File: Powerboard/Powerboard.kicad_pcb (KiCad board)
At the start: 2 copper layers, 44 parts, among them IC1 TEENSY_4.1, J1 Screw_Terminal_01x02, J3 Screw_Terminal_01x12, J4 Screw_Terminal_01x06, J5 Screw_Terminal_01x06, J6 Screw_Terminal_01x06, J7 Screw_Terminal_01x12, U1 MP2338GTL-Z, U3 MP2338GTL-Z, U5 SN74HCT245N, U6 SN74HCT245N, U7 SN74LVC245AN, U8 SN74LVC245AN

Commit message: Updated
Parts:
- removed C13: 100nF, Capacitor_SMD:C_0603_1608Metric
- removed C17, C19: 0.1uF, Capacitor_SMD:C_0603_1608Metric
- removed C18: 22nF, Capacitor_SMD:C_0603_1608Metric
- removed C20: 22uF, Capacitor_SMD:C_1206_3216Metric
- removed C21: 22uF, Capacitor_SMD:C_0603_1608Metric
- removed C22: 300pF, Capacitor_SMD:C_0603_1608Metric
- removed J7: Screw_Terminal_01x12, TerminalBlock_Phoenix:TerminalBlock_Phoenix_MKDS-1,5-12-5.08_1x12_P5.08mm_Horizontal
- removed L3: 6.8uH, Inductor_SMD:L_Bourns_SRP7028A_7.3x6.6mm
- removed R13: 191k, Resistor_SMD:R_0603_1608Metric
- removed R14: 49.9k, Resistor_SMD:R_0603_1608Metric
- removed R15, R16, R17: 10k, Resistor_SMD:R_0603_1608Metric
- removed R18: 90.9k, Resistor_SMD:R_0603_1608Metric
- removed R5: 9.09k, Resistor_SMD:R_0603_1608Metric
- removed R6: 51k, Resistor_SMD:R_0603_1608Metric
- removed U5, U6: SN74HCT245N, SN74HCT245N:N20
- removed U7, U8: SN74LVC245AN, SN74LVC245AN:N20
- added C10: 22uF, Capacitor_SMD:C_1206_3216Metric, F.Cu at (72.2, 87.5)
- added C9: 22uF, Capacitor_SMD:C_1206_3216Metric, F.Cu at (75.5, 87.5)
- added IC2: AP63301WU-7, AP63301WU:SOT95P280X100-6N, F.Cu at (61.5, 120.0)
- added IC3: AP63301WU-7, AP63301WU:SOT95P280X100-6N, F.Cu at (63.0, 90.0)
- added J2: Screw_Terminal_01x02, TerminalBlock_Altech:Altech_AK100_1x02_P5.00mm, F.Cu at (63.0, 140.0)
- added L2: 4.7uH, Inductor_SMD:L_Bourns_SRP7028A_7.3x6.6mm, F.Cu at (66.0, 82.0)
- added U2: SN74HCT245N, SN74HCT245N:N20, F.Cu at (169.8, 122.4)
- added U4: SN74LVC245AN, SN74LVC245AN:N20, F.Cu at (146.7, 122.4)
- C1: footprint Capacitor_SMD:C_1206_3216Metric -> Capacitor_SMD:C_1210_3225Metric
- C11: value 22uF -> 100nF; footprint Capacitor_SMD:C_1206_3216Metric -> Capacitor_SMD:C_0603_1608Metric
- C2: value 10uF -> 0.1uF; footprint Capacitor_SMD:C_1206_3216Metric -> Capacitor_SMD:C_0603_1608Metric
- C3: value 0.1uF -> 47pf
- C4: value 22nF -> 22uF; footprint Capacitor_SMD:C_0603_1608Metric -> Capacitor_SMD:C_1206_3216Metric
- C5: value 0.1uF -> 22uF; footprint Capacitor_SMD:C_0603_1608Metric -> Capacitor_SMD:C_1206_3216Metric
- C6: value 22uF -> 10uF; footprint Capacitor_SMD:C_1206_3216Metric -> Capacitor_SMD:C_1210_3225Metric
- C7: value 22uF -> 0.1uF; footprint Capacitor_SMD:C_1206_3216Metric -> Capacitor_SMD:C_0603_1608Metric
- C8: value 470pF -> 56pf; footprint Capacitor_SMD:C_0603_1608Metric -> Capacitor_SMD:C_0201_0603Metric
- J1: value Screw_Terminal_01x02 -> Screw_Terminal_01x06; footprint TerminalBlock_Altech:Altech_AK100_1x02_P5.00mm -> TerminalBlock_Phoenix:TerminalBlock_Phoenix_MPT-0,5-6-2.54_1x06_P2.54mm_Horizontal
- J3: value Screw_Terminal_01x12 -> 1993776; footprint TerminalBlock_Phoenix:TerminalBlock_Phoenix_MKDS-1,5-12-5.08_1x12_P5.08mm_Horizontal -> 1993776:PHOENIX_1993776
- J4, J5: value Screw_Terminal_01x06 -> Screw_Terminal_01x12; footprint TerminalBlock_Phoenix:TerminalBlock_Phoenix_MKDS-1,5-6_1x06_P5.00mm_Horizontal -> TerminalBlock_Phoenix:TerminalBlock_Phoenix_MPT-0,5-12-2.54_1x12_P2.54mm_Horizontal
- J6: value Screw_Terminal_01x06 -> 1993776; footprint TerminalBlock_Phoenix:TerminalBlock_Phoenix_MKDS-1,5-6_1x06_P5.00mm_Horizontal -> 1993776:PHOENIX_1993776
- R1: value 191k -> 30.1k
- R2: value 49.9k -> 158k
- R3: value 100k -> 30.1k
- R4: value 10k -> 93.1k
- U1: value MP2338GTL-Z -> SN74HCT245N; footprint MP2338GTL:SOT583_MP2338_MNP -> SN74HCT245N:N20
- U3: value MP2338GTL-Z -> SN74LVC245AN; footprint MP2338GTL:SOT583_MP2338_MNP -> SN74LVC245AN:N20
- moved C7 127.9 mm to (59.0, 84.5), turned to 90 degrees
- moved C2 123.0 mm to (56.5, 116.0), turned to 90 degrees
- moved R3 119.4 mm to (58.5, 91.5)
- moved R4 119.4 mm to (58.5, 94.0), turned to 180 degrees
- moved C6 117.5 mm to (65.5, 95.5)
- moved R2 116.8 mm to (58.0, 123.5), turned to 180 degrees
- moved C1 115.7 mm to (64.0, 125.5)
- moved C8 115.5 mm to (58.5, 96.7), turned to 180 degrees
- moved C3 113.0 mm to (58.0, 126.5), turned to 180 degrees
- moved R1 112.8 mm to (57.9, 121.3)
- moved L1 109.0 mm to (64.5, 112.5)
- moved C5 100.3 mm to (70.5, 115.5), turned to -90 degrees
- moved C4 96.7 mm to (74.0, 115.5), turned to -90 degrees
- moved J6 78.2 mm to (175.3, 85.9)
- moved C11 73.1 mm to (173.3, 98.0)
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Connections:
- C11 pad 1: /Step_down_3v3/Vin -> /Vout_5v
- C2 pad 1: /Step_down_3v3/Vin -> Net-(IC2-BST)
- C2 pad 2: GND -> Net-(IC2-SW)
- C3 pad 1: /Step_down_3v3/Vin -> Net-(IC2-FB)
- C3 pad 2: GND -> /Vout_5v
- C4 pad 1: Net-(U1-SS) -> /Vout_5v
- C5 pad 1: Net-(U1-SW) -> /Vout_5v
- C5 pad 2: Net-(U1-BST) -> GND
- C6 pad 1: /Vout_3v3 -> /Step_down_3v3/Vin
- C7 pad 1: /Vout_3v3 -> Net-(IC3-BST)
- C7 pad 2: GND -> Net-(IC3-SW)
- C8 pad 1: Net-(C8-Pad1) -> Net-(IC3-FB)
- J1 pad 1: /Step_down_3v3/Vin -> /SW1
- J1 pad 2: GND -> /SW2
- J4 pad 1: /Vout_3v3 -> /Motor Driver1/PUL1_5V
- J4 pad 2: /Vout_3v3 -> /Motor Driver1/DIR1_5v
- J4 pad 3: /Vout_3v3 -> /Motor Driver1/PUL2_5v
- J4 pad 4: /Vout_3v3 -> /Motor Driver1/DIR2_5v
- J4 pad 5: /Vout_3v3 -> /Motor Driver1/PUL3_5v
- J4 pad 6: /Vout_3v3 -> /Motor Driver1/DIR3_5v
- J5 pad 1: /SW1 -> /Encoder data1/EA1_5v
- J5 pad 2: /SW2 -> /Encoder data1/EB1_5v
- J5 pad 3: /SW3 -> /Encoder data1/EA2_5v
- J5 pad 4: /SW4 -> /Encoder data1/EB2_5v
- J5 pad 5: /SW5 -> /Encoder data1/EA3_5v
- J5 pad 6: /SW6 -> /Encoder data1/EB3_5v
- L1 pad 1: Net-(U1-SW) -> Net-(IC2-SW)
- L1 pad 2: /Vout_3v3 -> /Vout_5v
- R1 pad 1: /Step_down_3v3/Vin -> GND
- R1 pad 2: Net-(U1-EN) -> Net-(IC2-FB)
- R2 pad 1: Net-(U1-EN) -> Net-(IC2-FB)
- R2 pad 2: GND -> /Vout_5v
- R3 pad 1: Net-(U1-PG) -> GND
- R3 pad 2: /Vout_3v3 -> Net-(IC3-FB)
- R4 pad 1: Net-(C8-Pad1) -> Net-(IC3-FB)
- R4 pad 2: Net-(U1-FB) -> /Vout_3v3
- U1 pad 1: Net-(U1-PG) -> /Vout_5v
- U1 pad 2: /Step_down_3v3/Vin -> /PUL_1_3v3
- U1 pad 3: Net-(U1-SW) -> /DIR_1_3v3
- U1 pad 4: GND -> /PUL_2_3v3
- U1 pad 5: Net-(U1-BST) -> /DIR_2_3v3
- U1 pad 6: Net-(U1-EN) -> /PUL_3_3v3
- U1 pad 7: Net-(U1-SS) -> /DIR_3_3v3
- U1 pad 8: Net-(U1-FB) -> /PUL_4_3v3
- U3 pad 1: Net-(U3-PG) -> GND
- U3 pad 2: /Step_down_3v3/Vin -> /EA1_3v3
- U3 pad 3: Net-(U3-SW) -> /EB1_3v3
- U3 pad 4: GND -> /EA2_3v3
- U3 pad 5: Net-(U3-BST) -> /EB2_3v3
- U3 pad 6: Net-(U3-EN) -> /EA3_3v3
- U3 pad 7: Net-(U3-SS) -> /EB3_3v3
- U3 pad 8: Net-(U3-FB) -> /EA4_3v3
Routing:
- net /Step_down_3v3/Vin: track 0.00 -> 57.5 mm, vias 0 -> 1
- net /Vout_3v3: track 0.00 -> 29.2 mm, vias 0 -> 2
- net /Vout_5v: track 0.00 -> 28.4 mm, vias 0 -> 2
- net GND: vias 0 -> 21
- added copper zone on F.Cu, net (none)
- added copper zone on F.Cu, net /Step_down_3v3/Vin
- added copper zone on F.Cu, net /Vout_3v3
- added copper zone on F.Cu, net /Vout_5v
- added copper zone on B.Cu, net GND
- added copper zone on F.Cu, net Net-(IC2-BST)
- added copper zone on F.Cu, net Net-(IC2-FB)
- added copper zone on F.Cu, net Net-(IC2-SW)
- added copper zone on F.Cu, net Net-(IC3-BST)
- added copper zone on F.Cu, net Net-(IC3-FB)
- added copper zone on F.Cu, net Net-(IC3-SW)

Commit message: update
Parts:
- added H1: MountingHole, MountingHole:MountingHole_3.2mm_M3_Pad_Via, F.Cu at (51.5, 142.0)
- added H2: MountingHole, MountingHole:MountingHole_3.2mm_M3_Pad_Via, F.Cu at (140.2, 60.2)
- added H3: MountingHole, MountingHole:MountingHole_3.2mm_M3_Pad_Via, F.Cu at (214.5, 142.0)
- added H4: MountingHole, MountingHole:MountingHole_3.2mm_M3_Pad_Via, F.Cu at (214.2, 59.2)
- U1, U2: value SN74HCT245N -> SN74HCT245NSR; footprint SN74HCT245N:N20 -> SN74HCT245NSR:NS20
- U3, U4: value SN74LVC245AN -> SN74LVC245ADW; footprint SN74LVC245AN:N20 -> SN74LVC245ADW:DW20
- moved J1 81.9 mm to (192.4, 140.0)
- moved J5 78.1 mm to (81.4, 140.5)
- moved J4 69.7 mm to (124.8, 140.0)
- moved J6 58.5 mm to (177.1, 144.3)
- moved J3 58.0 mm to (163.1, 143.8)
- moved U3 47.1 mm to (89.0, 123.0), turned to -90 degrees
- moved U4 41.2 mm to (105.5, 123.0), turned to -90 degrees
- moved IC1 26.8 mm to (150.9, 85.1)
- moved U1 26.1 mm to (133.2, 120.6), turned to -90 degrees
- moved U2 20.4 mm to (149.5, 121.0), turned to -90 degrees
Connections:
- U1 pad 11: /Motor Driver1/DIR4_5v -> /Motor Driver1/PUL1_5V
- U1 pad 12: /Motor Driver1/PUL4_5v -> /Motor Driver1/DIR1_5v
- U1 pad 13: /Motor Driver1/DIR3_5v -> /Motor Driver1/PUL2_5v
- U1 pad 14: /Motor Driver1/PUL3_5v -> /Motor Driver1/DIR2_5v
- U1 pad 15: /Motor Driver1/DIR2_5v -> /Motor Driver1/PUL3_5v
- U1 pad 16: /Motor Driver1/PUL2_5v -> /Motor Driver1/DIR3_5v
- U1 pad 17: /Motor Driver1/DIR1_5v -> /Motor Driver1/PUL4_5v
- U1 pad 18: /Motor Driver1/PUL1_5V -> /Motor Driver1/DIR4_5v
- U1 pad 2: /PUL_1_3v3 -> /DIR_4_3v3
- U1 pad 3: /DIR_1_3v3 -> /PUL_4_3v3
- U1 pad 4: /PUL_2_3v3 -> /DIR_3_3v3
- U1 pad 5: /DIR_2_3v3 -> /PUL_3_3v3
- U1 pad 6: /PUL_3_3v3 -> /DIR_2_3v3
- U1 pad 7: /DIR_3_3v3 -> /PUL_2_3v3
- U1 pad 8: /PUL_4_3v3 -> /DIR_1_3v3
- U1 pad 9: /DIR_4_3v3 -> /PUL_1_3v3
- U2 pad 15: /Motor Driver1/DIR6_5v -> /Motor Driver1/PUL5_5v
- U2 pad 16: /Motor Driver1/PUL6_5v -> /Motor Driver1/DIR5_5v
- U2 pad 17: /Motor Driver1/DIR5_5v -> /Motor Driver1/PUL6_5v
- U2 pad 18: /Motor Driver1/PUL5_5v -> /Motor Driver1/DIR6_5v
- U2 pad 2: /PUL_5_3v3 -> /DIR_6_3v3
- U2 pad 3: /DIR_5_3v3 -> /PUL_6_3v3
- U2 pad 4: /PUL_6_3v3 -> /DIR_5_3v3
- U2 pad 5: /DIR_6_3v3 -> /PUL_5_3v3
- U3 pad 11: /Encoder data1/EB4_5v -> /Encoder data1/EA1_5v
- U3 pad 12: /Encoder data1/EA4_5v -> /Encoder data1/EB1_5v
- U3 pad 13: /Encoder data1/EB3_5v -> /Encoder data1/EA2_5v
- U3 pad 14: /Encoder data1/EA3_5v -> /Encoder data1/EB2_5v
- U3 pad 15: /Encoder data1/EB2_5v -> /Encoder data1/EA3_5v
- U3 pad 16: /Encoder data1/EA2_5v -> /Encoder data1/EB3_5v
- U3 pad 17: /Encoder data1/EB1_5v -> /Encoder data1/EA4_5v
- U3 pad 18: /Encoder data1/EA1_5v -> /Encoder data1/EB4_5v
- U3 pad 2: /EA1_3v3 -> /EB4_3v3
- U3 pad 3: /EB1_3v3 -> /EA4_3v3
- U3 pad 4: /EA2_3v3 -> /EB3_3v3
- U3 pad 5: /EB2_3v3 -> /EA3_3v3
- U3 pad 6: /EA3_3v3 -> /EB2_3v3
- U3 pad 7: /EB3_3v3 -> /EA2_3v3
- U3 pad 8: /EA4_3v3 -> /EB1_3v3
- U3 pad 9: /EB4_3v3 -> /EA1_3v3
- U4 pad 15: /Encoder data1/EB6_5v -> /Encoder data1/EA5_5v
- U4 pad 16: /Encoder data1/EA6_5v -> /Encoder data1/EB5_5v
- U4 pad 17: /Encoder data1/EB5_5v -> /Encoder data1/EA6_5v
- U4 pad 18: /Encoder data1/EA5_5v -> /Encoder data1/EB6_5v
- U4 pad 2: /EA5_3v3 -> /EB6_3v3
- U4 pad 3: /EB5_3v3 -> /EA6_3v3
- U4 pad 4: /EA6_3v3 -> /EB5_3v3
- U4 pad 5: /EB6_3v3 -> /EA5_3v3
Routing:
- net /Step_down_3v3/Vin: track 57.5 -> 55.0 mm
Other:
- board outline added: 170 x 90 mm

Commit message: Pre-DRC Done
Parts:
- H1, H2, H3, H4: footprint MountingHole:MountingHole_3.2mm_M3_Pad_Via -> MountingHole:MountingHole_3.2mm_M3_Pad
- moved C11 56.0 mm to (128.1, 131.0), turned to 180 degrees
- moved C12 41.9 mm to (145.1, 131.5), turned to 180 degrees
- moved IC1 14.8 mm to (143.9, 98.1)
- moved U1 10.9 mm to (122.7, 123.6)
- moved U2 10.2 mm to (139.6, 123.5)
- moved J4 8.26 mm to (116.6, 140.5)
- moved J6 7.05 mm to (170.1, 143.8)
- moved J3 7.00 mm to (156.1, 143.8)
- moved J2 0.50 mm to (63.0, 139.5)
- moved U4 0.50 mm to (106.0, 123.0)
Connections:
- IC1 pad 16: /EB4_3v3 -> /EA1_3v3
- IC1 pad 17: /EA4_3v3 -> /EB1_3v3
- IC1 pad 18: /EB3_3v3 -> /EA2_3v3
- IC1 pad 19: /EA3_3v3 -> /EB2_3v3
- IC1 pad 20: /EB2_3v3 -> /EA3_3v3
- IC1 pad 21: /EA2_3v3 -> /EB3_3v3
- IC1 pad 22: /EB1_3v3 -> /EA4_3v3
- IC1 pad 23: /EA1_3v3 -> /EB4_3v3
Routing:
- net /Vout_3v3: track 29.2 -> 212.4 mm, vias 2 -> 4
- net /Vout_5v: track 28.4 -> 202.8 mm, vias 2 -> 5
- net GND: track 0.00 -> 137.8 mm, vias 21 -> 26
- net /EA1_3v3: track 0.00 -> 111.3 mm
- net /EB1_3v3: track 0.00 -> 105.8 mm
- net /EA2_3v3: track 0.00 -> 100.4 mm
- net /EB2_3v3: track 0.00 -> 93.6 mm
- net /EB6_3v3: track 0.00 -> 89.2 mm
- net /EA6_3v3: track 0.00 -> 89.1 mm
- net /EA3_3v3: track 0.00 -> 88.0 mm
- net /EB5_3v3: track 0.00 -> 82.5 mm
- net /EB3_3v3: track 0.00 -> 82.1 mm
- net /EA5_3v3: track 0.00 -> 79.9 mm
- net /EA4_3v3: track 0.00 -> 76.4 mm
- net /EB4_3v3: track 0.00 -> 71.6 mm
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- removed copper zone on F.Cu, net (none)

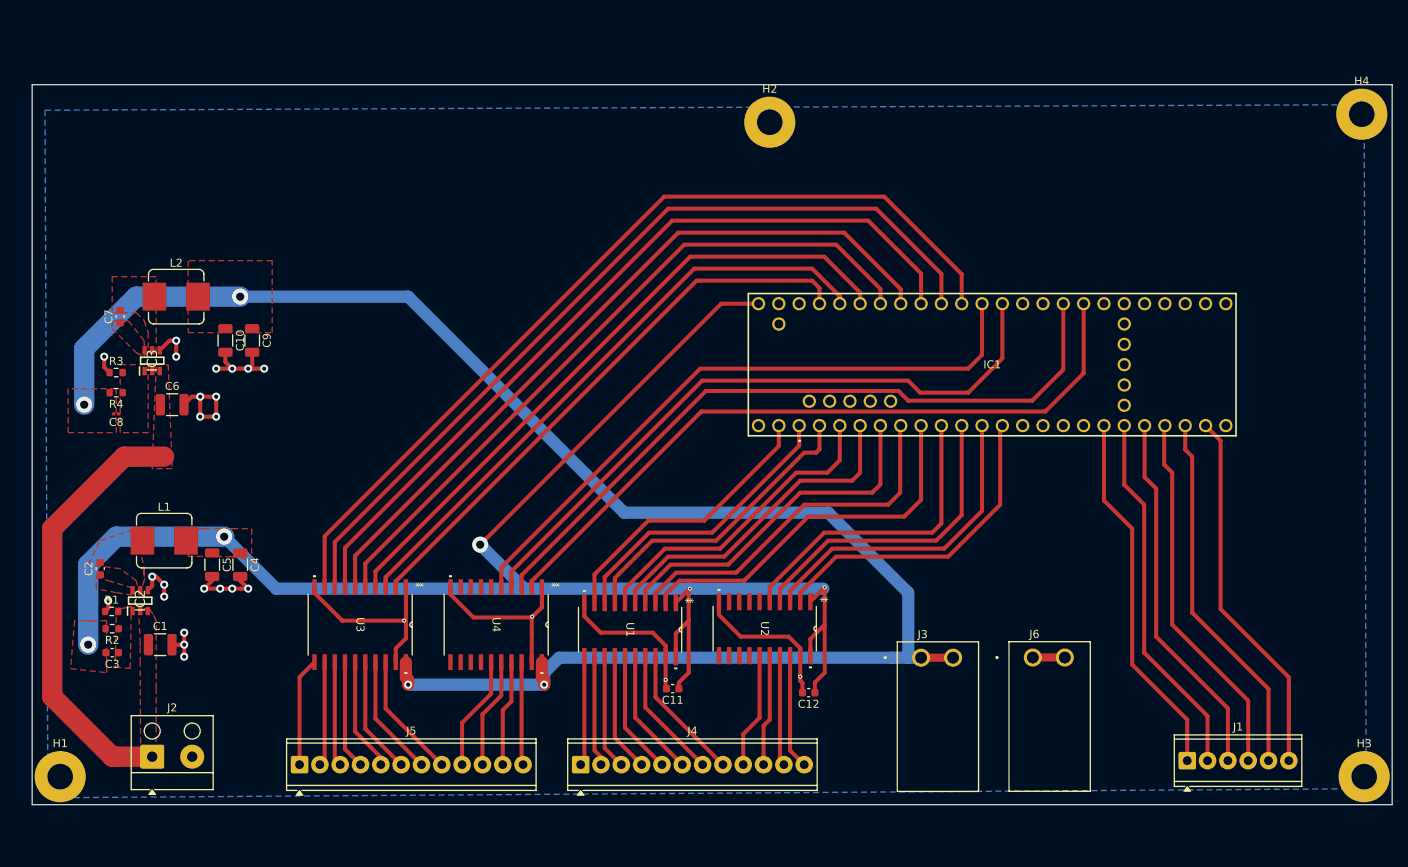
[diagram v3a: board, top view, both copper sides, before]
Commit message: Rev1.1 Done
Finished the board ran DRC all clear
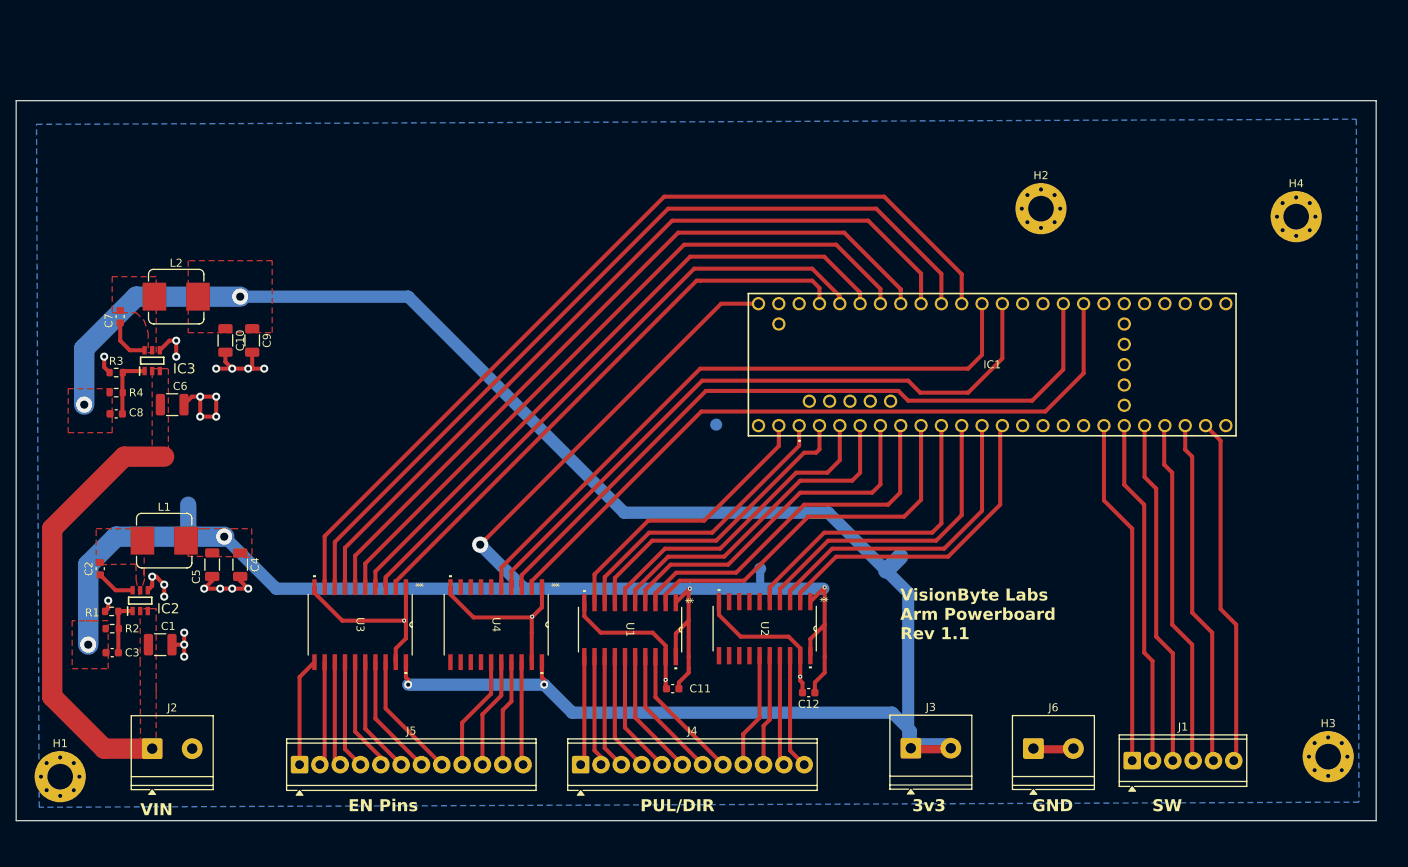
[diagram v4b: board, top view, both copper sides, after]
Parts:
- added TP1: TestPoint, TestPoint:TestPoint_Pad_D1.5mm, B.Cu at (133.5, 98.0)
- added TP2: TestPoint, TestPoint:TestPoint_Pad_D1.5mm, B.Cu at (139.0, 116.0)
- added TP3: TestPoint, TestPoint:TestPoint_Pad_D1.5mm, B.Cu at (156.5, 114.5)
- added TP4: TestPoint, TestPoint:TestPoint_Pad_D1.5mm, B.Cu at (67.5, 108.0)
- C8: footprint Capacitor_SMD:C_0201_0603Metric -> Capacitor_SMD:C_0603_1608Metric
- H1, H2, H3, H4: footprint MountingHole:MountingHole_3.2mm_M3_Pad -> MountingHole:MountingHole_3.2mm_M3_Pad_Via
- J2: footprint TerminalBlock_Altech:Altech_AK100_1x02_P5.00mm -> TerminalBlock_Phoenix:TerminalBlock_Phoenix_PT-1,5-2-5.0-H_1x02_P5.00mm_Horizontal
- J3, J6: value 1993776 -> Screw_Terminal_01x02; footprint 1993776:PHOENIX_1993776 -> TerminalBlock_Phoenix:TerminalBlock_Phoenix_PT-1,5-2-5.0-H_1x02_P5.00mm_Horizontal
- moved H2 35.6 mm to (174.1, 71.0)
- moved H4 15.2 mm to (206.0, 72.0)
- moved J1 6.88 mm to (185.5, 140.0)
- moved J6 6.15 mm to (173.2, 138.5)
- moved J3 5.67 mm to (157.8, 138.4)
- moved H3 5.15 mm to (210.0, 139.5)
- moved J2 1.00 mm to (63.0, 138.5)
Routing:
- net /Vout_3v3: track 212.4 -> 232.3 mm
- net Net-(IC3-FB): track 0.00 -> 7.98 mm
- net Net-(IC2-FB): track 0.00 -> 6.96 mm
- net /Vout_5v: track 202.8 -> 209.3 mm
- net Net-(IC3-BST): track 0.00 -> 5.77 mm
- net Net-(IC2-BST): track 0.00 -> 4.85 mm
- net /SW5: track 46.2 -> 43.3 mm
- net /SW4: track 46.3 -> 43.4 mm
- net /SW3: track 46.2 -> 43.3 mm
- net /SW2: track 46.2 -> 43.3 mm
- net /SW1: track 46.2 -> 43.3 mm
- net /SW6: track 46.2 -> 43.6 mm
- removed copper zone on F.Cu, net Net-(IC2-BST)
- removed copper zone on F.Cu, net Net-(IC2-FB)
- removed copper zone on F.Cu, net Net-(IC3-BST)
- removed copper zone on F.Cu, net Net-(IC3-FB)
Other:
- board text added: "3v3"
- board text added: "EN Pins"
- board text added: "GND"
- board text added: "PUL/DIR"
- board text added: "SW"
- board text added: "VIN"
- board text added: "VisionByte Labs Arm Powerboard Rev 1.1"

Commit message: Replaced HCT->ACT
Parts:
- added J7: Screw_Terminal_01x02, TerminalBlock_Phoenix:TerminalBlock_Phoenix_MPT-0,5-2-2.54_1x02_P2.54mm_Horizontal, F.Cu at (172.2, 111.5)
- U1, U2: value SN74HCT245NSR -> SN74ACT245NSR; footprint SN74HCT245NSR:NS20 -> SN74ACT245NSR:NS20
- moved U2 0.62 mm to (139.6, 124.1)
- moved U1 0.26 mm to (122.8, 123.4)
- renumbered TP2 to TP1, TP3 to TP2, TP1 to TP3
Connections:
- IC1 pad 24: unconnected-(IC1-A10-Pad24) -> Net-(IC1-A10)
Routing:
- net Net-(IC1-A10): track 0.00 -> 14.3 mm
